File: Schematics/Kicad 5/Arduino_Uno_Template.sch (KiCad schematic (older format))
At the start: 0 parts

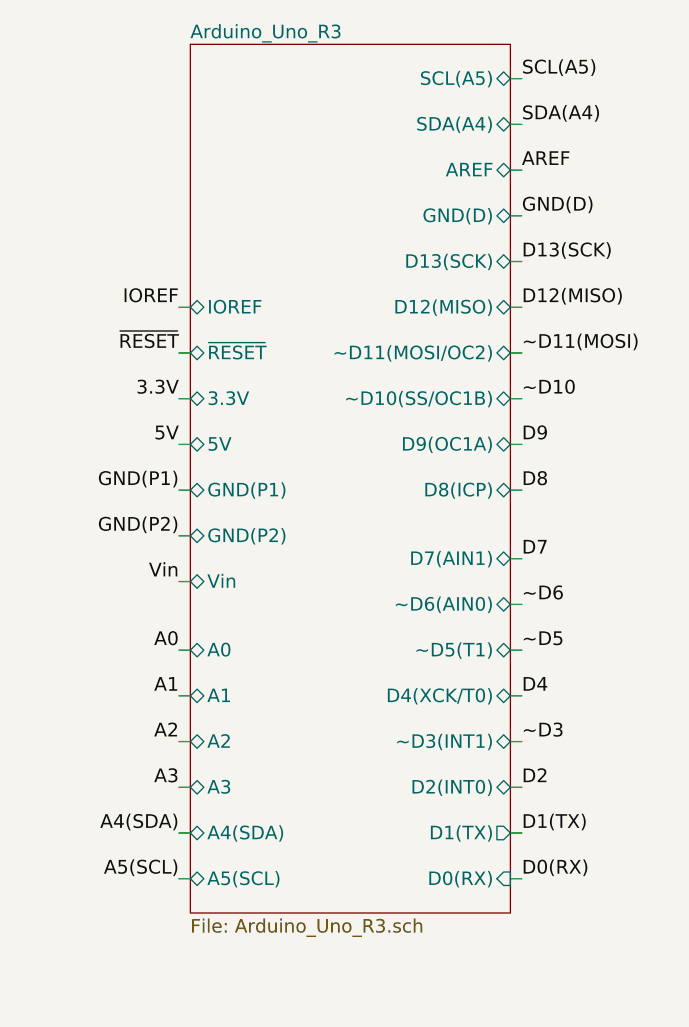
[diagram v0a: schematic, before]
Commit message: addded Arduino_Uno_Header symbol
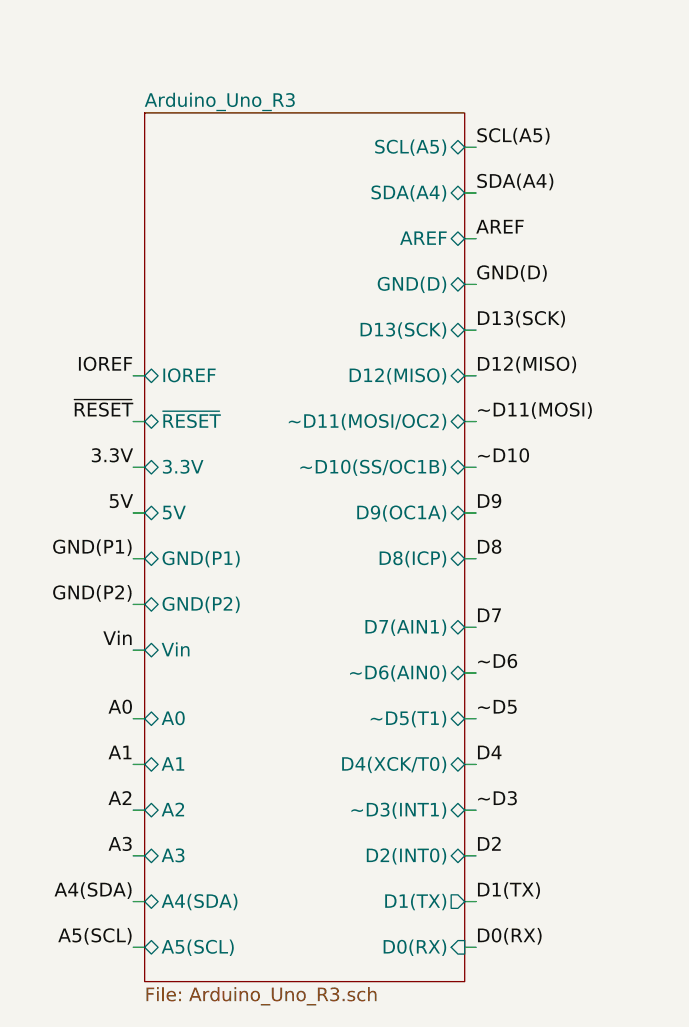
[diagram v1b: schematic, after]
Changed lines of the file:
@@
 $EndDescr
 $Sheet
-S 13950 650  1400 3800
+S 13750 950  1400 3800
 U 55DD0855
 F0 "Arduino_Uno_R3" 59
 F1 "Arduino_Uno_R3.sch" 59
-F2 "D0(RX)" I R 15350 4300 59
-F3 "D1(TX)" O R 15350 4100 59
-F4 "D2(INT0)" B R 15350 3900 59
-F5 "~~D3(INT1)" B R 15350 3700 59
-F6 "D4(XCK/T0)" B R 15350 3500 59
-F7 "~~D5(T1)" B R 15350 3300 59
-F8 "~~D6(AIN0)" B R 15350 3100 59
-F9 "D7(AIN1)" B R 15350 2900 59
-F10 "D8(ICP)" B R 15350 2600 59
-F11 "D9(OC1A)" B R 15350 2400 59
-F12 "~~D10(SS/OC1B)" B R 15350 2200 59
-F13 "~~D11(MOSI/OC2)" B R 15350 2000 59
-F14 "D12(MISO)" B R 15350 1800 59
-F15 "D13(SCK)" B R 15350 1600 59
-F16 "GND(D)" B R 15350 1400 59
-F17 "AREF" B R 15350 1200 59
-F18 "SDA(A4)" B R 15350 1000 59
-F19 "SCL(A5)" B R 15350 800 59
-F20 "IOREF" B L 13950 1800 59
-F21 "~RESET" B L 13950 2000 59
-F22 "3.3V" B L 13950 2200 59
-F23 "5V" B L 13950 2400 59
-F24 "GND(P1)" B L 13950 2600 59
-F25 "GND(P2)" B L 13950 2800 59
-F26 "Vin" B L 13950 3000 59
-F27 "A0" B L 13950 3300 59
-F28 "A1" B L 13950 3500 59
-F29 "A2" B L 13950 3700 59
-F30 "A3" B L 13950 3900 59
-F31 "A4(SDA)" B L 13950 4100 59
-F32 "A5(SCL)" B L 13950 4300 59
+F2 "D0(RX)" I R 15150 4600 59
+F3 "D1(TX)" O R 15150 4400 59
+F4 "D2(INT0)" B R 15150 4200 59
+F5 "~~D3(INT1)" B R 15150 4000 59
+F6 "D4(XCK/T0)" B R 15150 3800 59
+F7 "~~D5(T1)" B R 15150 3600 59
+F8 "~~D6(AIN0)" B R 15150 3400 59
+F9 "D7(AIN1)" B R 15150 3200 59
+F10 "D8(ICP)" B R 15150 2900 59
+F11 "D9(OC1A)" B R 15150 2700 59
+F12 "~~D10(SS/OC1B)" B R 15150 2500 59
+F13 "~~D11(MOSI/OC2)" B R 15150 2300 59
+F14 "D12(MISO)" B R 15150 2100 59
+F15 "D13(SCK)" B R 15150 1900 59
+F16 "GND(D)" B R 15150 1700 59
+F17 "AREF" B R 15150 1500 59
+F18 "SDA(A4)" B R 15150 1300 59
+F19 "SCL(A5)" B R 15150 1100 59
+F20 "IOREF" B L 13750 2100 59
+F21 "~RESET" B L 13750 2300 59
+F22 "3.3V" B L 13750 2500 59
+F23 "5V" B L 13750 2700 59
+F24 "GND(P1)" B L 13750 2900 59
+F25 "GND(P2)" B L 13750 3100 59
+F26 "Vin" B L 13750 3300 59
+F27 "A0" B L 13750 3600 59
+F28 "A1" B L 13750 3800 59
+F29 "A2" B L 13750 4000 59
+F30 "A3" B L 13750 4200 59
+F31 "A4(SDA)" B L 13750 4400 59
+F32 "A5(SCL)" B L 13750 4600 59
 $EndSheet
-Text Label 15400 3900 0    60   ~ 0
+Text Label 15200 4200 0    60   ~ 0
 D2
-Text Label 15400 3700 0    60   ~ 0
+Text Label 15200 4000 0    60   ~ 0
 ~~D3
-Text Label 15400 3500 0    60   ~ 0
+Text Label 15200 3800 0    60   ~ 0
 D4
-Text Label 15400 3300 0    60   ~ 0
+Text Label 15200 3600 0    60   ~ 0
 ~~D5
-Text Label 15400 3100 0    60   ~ 0
+Text Label 15200 3400 0    60   ~ 0
 ~~D6
-Text Label 15400 2900 0    60   ~ 0
+Text Label 15200 3200 0    60   ~ 0
 D7
-Text Label 15400 4300 0    60   ~ 0
+Text Label 15200 4600 0    60   ~ 0
 D0(RX)
-Text Label 15400 4100 0    60   ~ 0
+Text Label 15200 4400 0    60   ~ 0
 D1(TX)
 Wire Wire Line
-	15350 4300 15400 4300
-Text Label 15400 2600 0    60   ~ 0
+	15150 4600 15200 4600
+Text Label 15200 2900 0    60   ~ 0
 D8
-Text Label 15400 2400 0    60   ~ 0
+Text Label 15200 2700 0    60   ~ 0
 D9
-Text Label 15400 2200 0    60   ~ 0
+Text Label 15200 2500 0    60   ~ 0
 ~~D10
-Text Label 15400 2000 0    60   ~ 0
+Text Label 15200 2300 0    60   ~ 0
 ~~D11(MOSI)
-Text Label 15400 1800 0    60   ~ 0
+Text Label 15200 2100 0    60   ~ 0
 D12(MISO)
-Text Label 15400 1600 0    60   ~ 0
+Text Label 15200 1900 0    60   ~ 0
 D13(SCK)
-Text Label 15400 1200 0    60   ~ 0
+Text Label 15200 1500 0    60   ~ 0
 AREF
-Text Label 15400 1000 0    60   ~ 0
+Text Label 15200 1300 0    60   ~ 0
 SDA(A4)
-Text Label 15400 800  0    60   ~ 0
+Text Label 15200 1100 0    60   ~ 0
 SCL(A5)
 Wire Wire Line
-	15350 4100 15400 4100
+	15150 4400 15200 4400
 Wire Wire Line
-	15350 3900 15400 3900
+	15150 4200 15200 4200
 Wire Wire Line
-	15350 3700 15400 3700
+	15150 4000 15200 4000
 Wire Wire Line
-	15350 3500 15400 3500
+	15150 3800 15200 3800
 Wire Wire Line
-	15350 3300 15400 3300
+	15150 3600 15200 3600
 Wire Wire Line
-	15350 3100 15400 3100
+	15150 3400 15200 3400
 Wire Wire Line
-	15350 2900 15400 2900
+	15150 3200 15200 3200
 Wire Wire Line
-	15350 2600 15400 2600
+	15150 2900 15200 2900
 Wire Wire Line
-	15350 2400 15400 2400
+	15150 2700 15200 2700
 Wire Wire Line
-	15350 2200 15400 2200
+	15150 2500 15200 2500
 Wire Wire Line
-	15350 2000 15400 2000
+	15150 2300 15200 2300
 Wire Wire Line
-	15350 1800 15400 1800
+	15150 2100 15200 2100
 Wire Wire Line
-	15350 1600 15400 1600
+	15150 1900 15200 1900
 Wire Wire Line
-	15350 1400 15400 1400
+	15150 1700 15200 1700
 Wire Wire Line
-	15350 1200 15400 1200
+	15150 1500 15200 1500
 Wire Wire Line
-	15350 1000 15400 1000
+	15150 1300 15200 1300
 Wire Wire Line
-	15350 800  15400 800
-Text Label 15400 1400 0    60   ~ 0
+	15150 1100 15200 1100
+Text Label 15200 1700 0    60   ~ 0
 GND(D)
-Text Label 13900 3300 2    60   ~ 0
+Text Label 13700 3600 2    60   ~ 0
 A0
-Text Label 13900 3500 2    60   ~ 0
+Text Label 13700 3800 2    60   ~ 0
 A1
-Text Label 13900 3700 2    60   ~ 0
+Text Label 13700 4000 2    60   ~ 0
 A2
-Text Label 13900 3900 2    60   ~ 0
+Text Label 13700 4200 2    60   ~ 0
 A3
-Text Label 13900 4100 2    60   ~ 0
+Text Label 13700 4400 2    60   ~ 0
 A4(SDA)
-Text Label 13900 4300 2    60   ~ 0
+Text Label 13700 4600 2    60   ~ 0
 A5(SCL)
 Wire Wire Line
-	13900 4300 13950 4300
+	13700 4600 13750 4600
 Wire Wire Line
-	13900 4100 13950 4100
+	13700 4400 13750 4400
 Wire Wire Line
-	13900 3900 13950 3900
+	13700 4200 13750 4200
 Wire Wire Line
-	13900 3700 13950 3700
+	13700 4000 13750 4000
 Wire Wire Line
-	13900 3500 13950 3500
+	13700 3800 13750 3800
 Wire Wire Line
-	13900 3300 13950 3300
-Text Label 13900 2000 2    60   ~ 0
+	13700 3600 13750 3600
+Text Label 13700 2300 2    60   ~ 0
 ~RESET
-Text Label 13900 2200 2    60   ~ 0
+Text Label 13700 2500 2    60   ~ 0
 3.3V
-Text Label 13900 2400 2    60   ~ 0
+Text Label 13700 2700 2    60   ~ 0
 5V
-Text Label 13900 2600 2    60   ~ 0
+Text Label 13700 2900 2    60   ~ 0
 GND(P1)
-Text Label 13900 2800 2    60   ~ 0
+Text Label 13700 3100 2    60   ~ 0
 GND(P2)
-Text Label 13900 3000 2    60   ~ 0
+Text Label 13700 3300 2    60   ~ 0
 Vin
 Wire Wire Line
-	13900 3000 13950 3000
+	13700 3300 13750 3300
 Wire Wire Line
-	13900 2800 13950 2800
+	13700 3100 13750 3100
 Wire Wire Line
-	13900 2600 13950 2600
+	13700 2900 13750 2900
 Wire Wire Line
-	13900 2400 13950 2400
+	13700 2700 13750 2700
 Wire Wire Line
-	13900 2200 13950 2200
+	13700 2500 13750 2500
 Wire Wire Line
-	13900 2000 13950 2000
-Text Label 13900 1800 2    60   ~ 0
+	13700 2300 13750 2300
+Text Label 13700 2100 2    60   ~ 0
 IOREF
 Wire Wire Line
-	13900 1800 13950 1800
+	13700 2100 13750 2100
 $EndSCHEMATC
